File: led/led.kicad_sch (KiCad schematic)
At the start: 14 parts, among them SW1 SW_Push, SW2 SW_Push, U1 74HC595, U2 74HC138

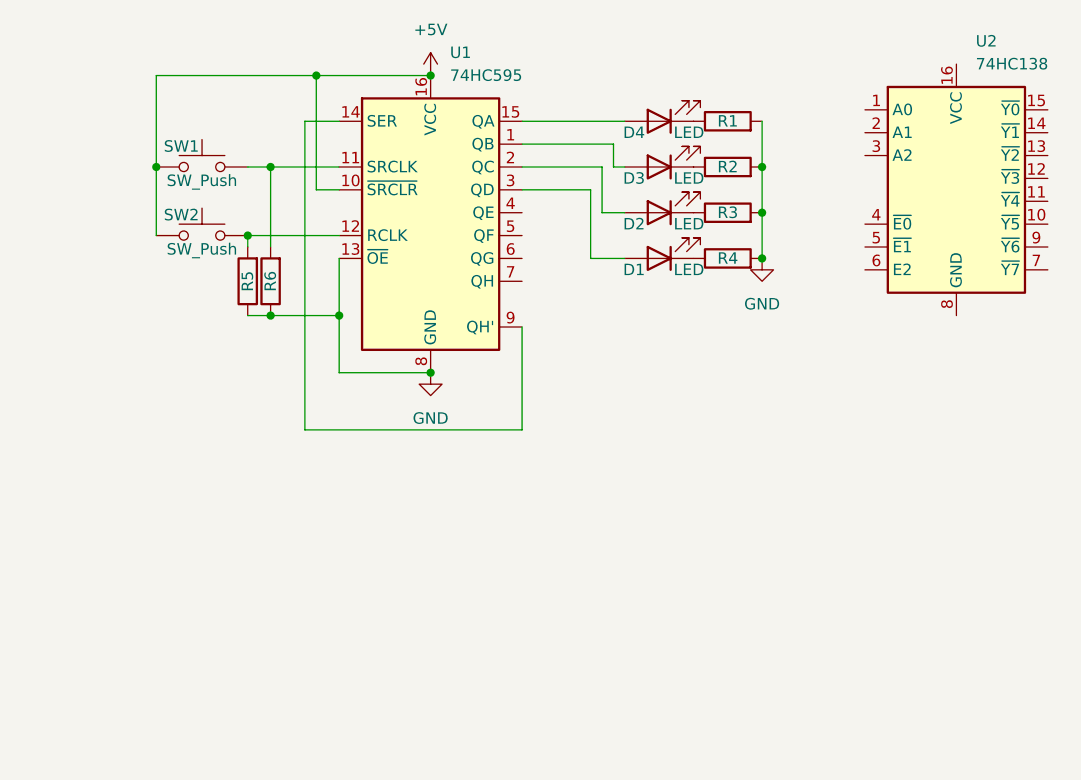
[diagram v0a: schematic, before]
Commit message: bus support, more demo projects
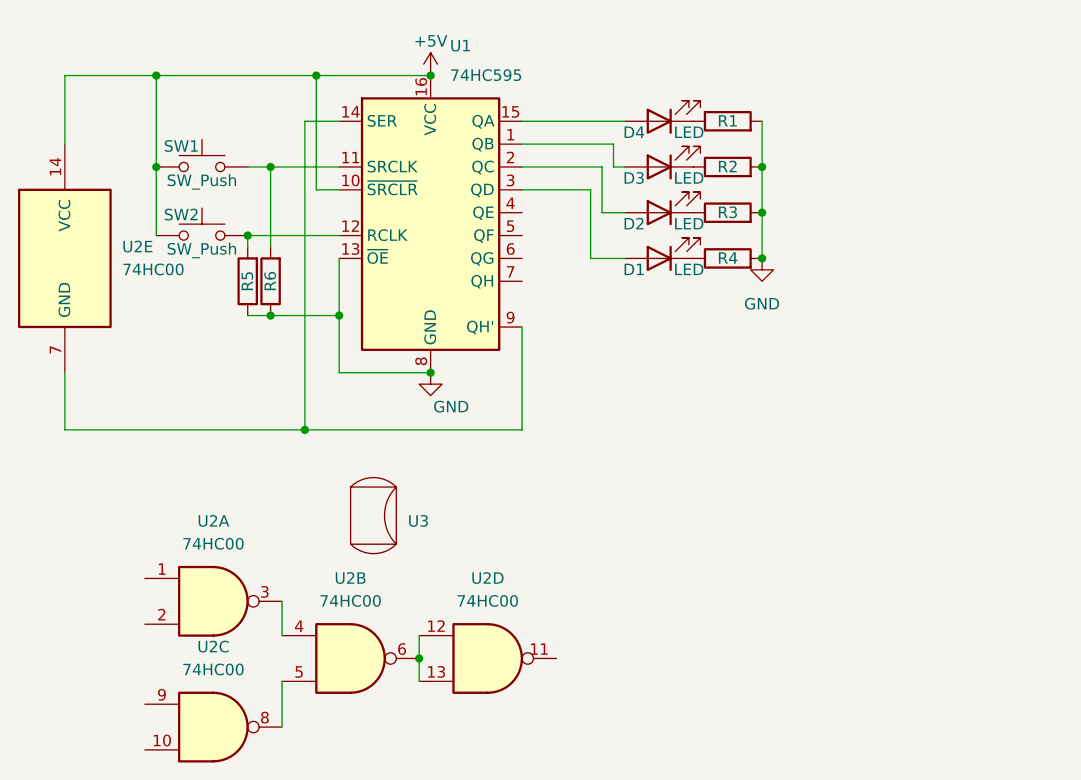
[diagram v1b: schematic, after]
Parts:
- removed U2: 74HC138, Package_DIP:DIP-16_W7.62mm_LongPads, symbol 74xx:74HC138
- added U2: 74HC00, symbol 74xx:74HC00
- added U3: (no value), symbol test_arc:bogolau2
- U1: footprint Package_DIP:DIP-16_W7.62mm_LongPads -> (none)
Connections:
- net +5V: now also U2.14 (VCC)
- net at U1.14 (SER), U1.9 (QH'): now also U2.7 (GND)
- new net: U2.12, U2.13, U2.6
- new net: U2.5, U2.8
- new net: U2.3, U2.4
